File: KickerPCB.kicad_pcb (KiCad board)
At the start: 2 copper layers, 68 x 52.8 mm, 19 parts, among them J1 Conn_01x03_Pin, U1 30k, U10 N channel, U11 D, U12 10K, U13 Conn_01x02, U14 2200, U2 115k, U3 BSP89, U4 Optocoupler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

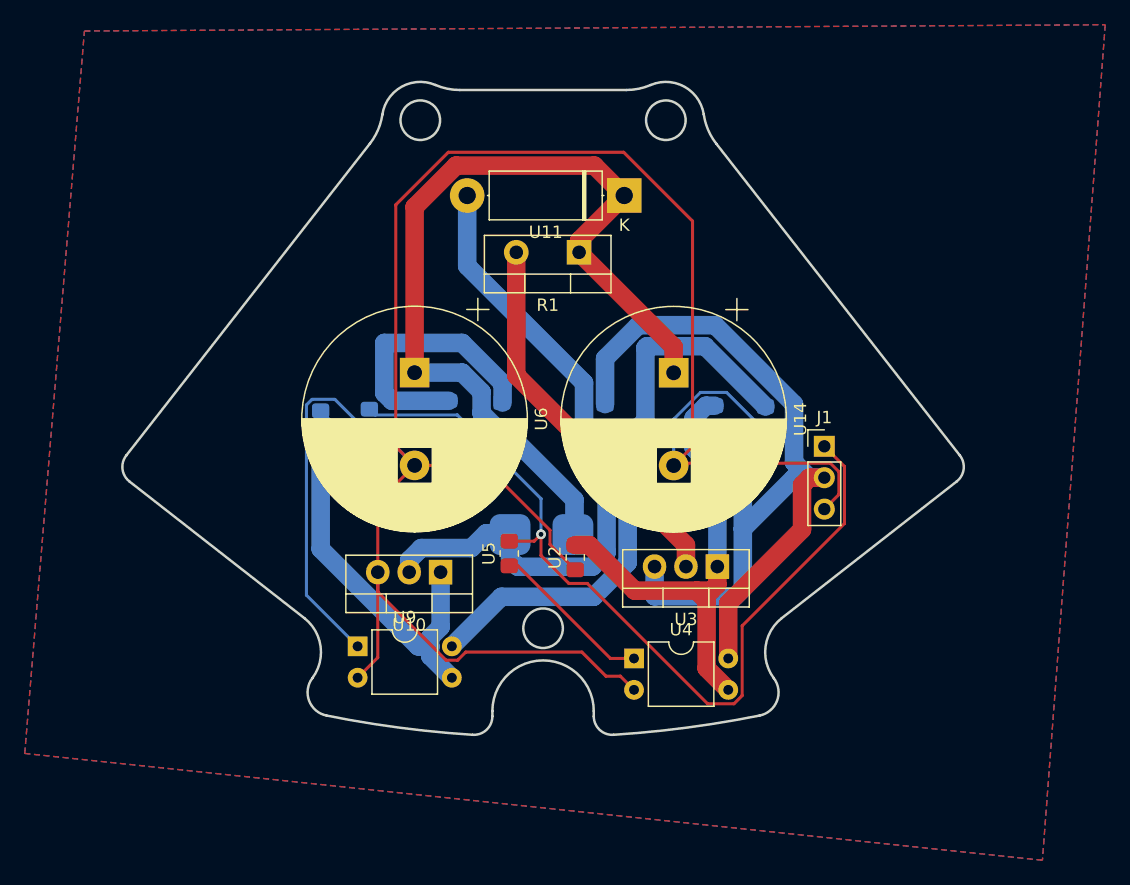
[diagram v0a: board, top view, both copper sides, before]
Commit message: Moved Caps
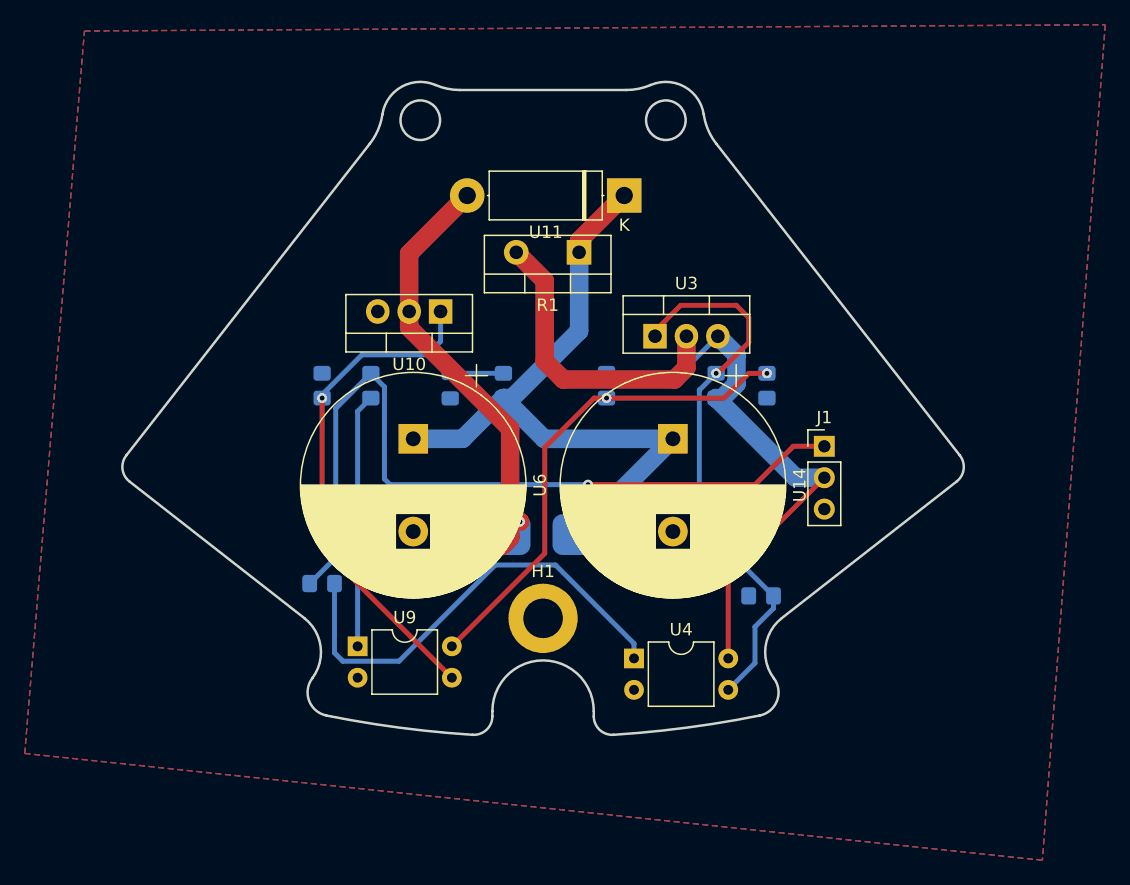
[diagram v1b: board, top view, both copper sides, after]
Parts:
- added H1: MountingHole, MountingHole:MountingHole_3.2mm_M3_DIN965_Pad, F.Cu at (96.9, 84.8)
- U2, U5: moved to B.Cu
- moved U10 21.1 mm to (88.6, 60.0)
- moved U3 19.3 mm to (105.9, 62.0), turned to 0 degrees
- moved U2 15.3 mm to (114.5, 83.0), turned to 0 degrees
- moved U5 15.3 mm to (79.0, 82.0), turned to 180 degrees
- moved U6 9.10 mm to (86.4, 74.0)
- moved U14 9.09 mm to (107.4, 74.0)
- moved U12 3.03 mm to (79.0, 66.0)
- moved U8 2.90 mm to (82.9, 66.0)
- moved R3 2.69 mm to (115.0, 66.0)
- moved U1 2.62 mm to (110.9, 66.0)
- moved R2 2.49 mm to (102.0, 66.0)
- moved U7 2.36 mm to (93.7, 66.0)
- moved D1 2.25 mm to (89.4, 66.0)
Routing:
- net GND: track 182.8 -> 0.00 mm
- net 48V: track 80.8 -> 46.2 mm
- net Net-(U4-A): track 13.2 -> 37.2 mm
- net Net-(U10-S): track 54.2 -> 35.7 mm, vias 0 -> 4
- net Net-(D1-A): track 22.0 -> 4.31 mm
- net Net-(U11-K): track 72.8 -> 55.9 mm
- net 12V: track 49.8 -> 39.6 mm, vias 0 -> 2
- net Net-(U10-G): track 30.9 -> 41.0 mm, vias 0 -> 1
- net Net-(U9-A): track 27.7 -> 20.5 mm
- net Net-(U3-G): track 38.7 -> 45.1 mm, vias 0 -> 1
- net Net-(U3-D): track 31.1 -> 24.8 mm
- net Kicker: track 70.1 -> 65.1 mm
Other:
- outline, holes or cut-outs redrawn
